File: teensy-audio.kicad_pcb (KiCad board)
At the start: 2 copper layers, 80 x 140 mm, 47 parts, among them J1 AudioJack2, J10 Conn_01x05, J11 Conn_01x02, J2 AudioJack2, J3 Barrel_Jack, J4 Conn_02x08_Odd_Even, J5 Conn_02x08_Odd_Even, J6 Conn_02x05_Odd_Even, J7 Conn_01x04, J8 Conn_01x04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

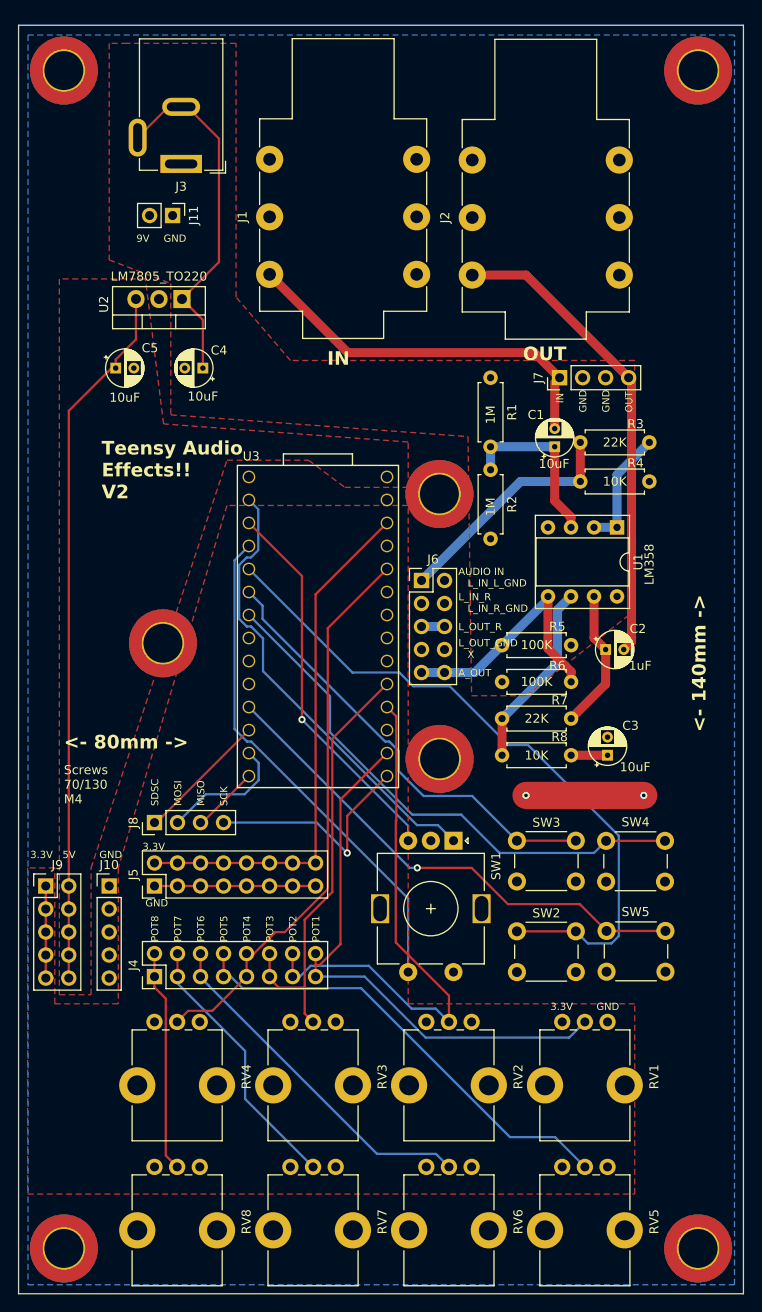
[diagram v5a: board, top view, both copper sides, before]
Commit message: added pin nubmers to silkscreen
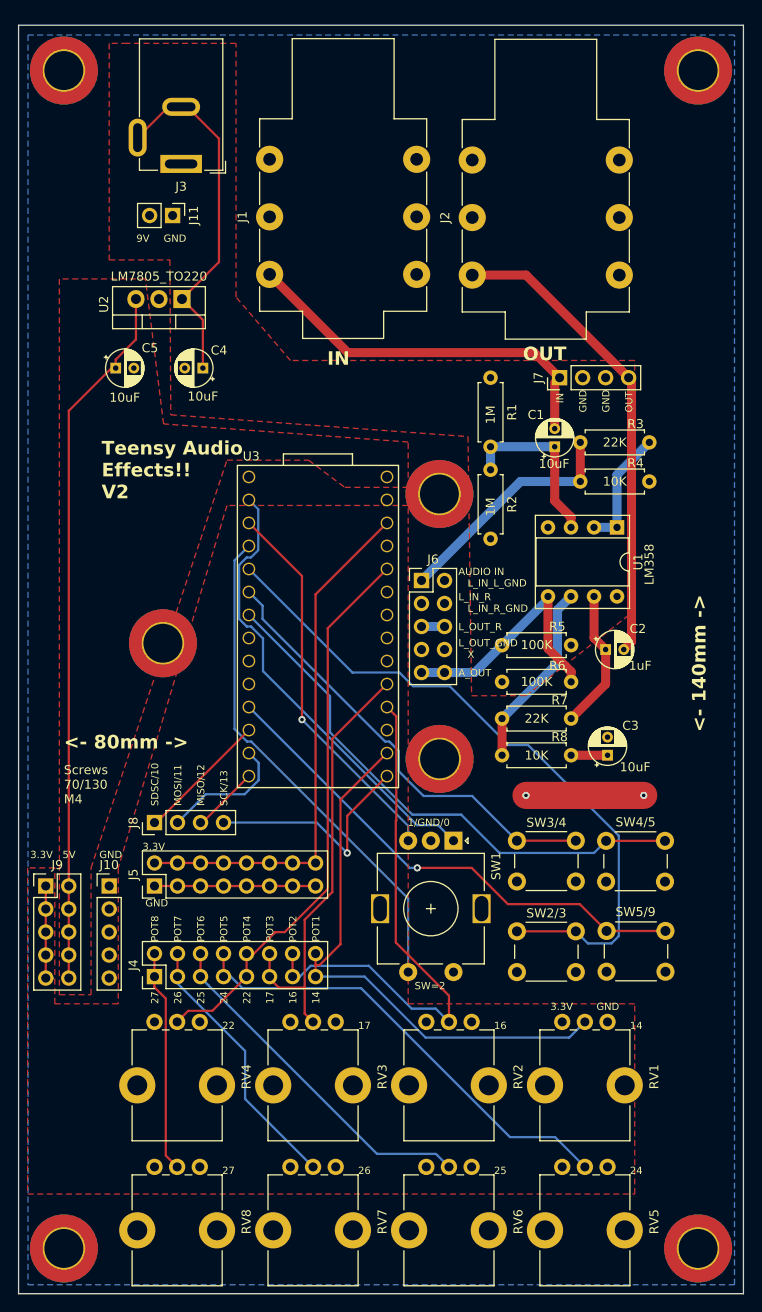
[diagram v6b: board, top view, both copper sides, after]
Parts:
- renumbered SW2 to SW2/3, SW3 to SW3/4, SW4 to SW4/5, SW5 to SW5/9
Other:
- board text added: "1/GND/0"
- board text added: "14"
- board text added: "16"
- board text added: "17"
- board text added: "22"
- board text added: "24"
- board text added: "25"
- board text added: "26"
- board text added: "27"
- board text added: "MISO/12"
- board text added: "MOSI/11"
- board text added: "SCK/13"
- board text added: "SDSC/10"
- board text added: "SW=2"
- board text removed: "MISO"
- board text removed: "MOSI"
- board text removed: "SCK"
- board text removed: "SDSC"
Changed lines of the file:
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@@
     (property "ki_keywords" "switch normally-open pushbutton push-button")
     (attr through_hole)
-    (fp_text reference "SW5" (at 3.302 6.604) (layer "F.SilkS")
+    (fp_text reference "SW5/9" (at 3.302 6.604) (layer "F.SilkS")
         (effects (font (size 1 1) (thickness 0.15)))
     )
@@
     (property "ki_keywords" "switch normally-open pushbutton push-button")
     (attr through_hole)
-    (fp_text reference "SW3" (at 3.25 -2) (layer "F.SilkS")
+    (fp_text reference "SW3/4" (at 3.25 -2) (layer "F.SilkS")
         (effects (font (size 1 1) (thickness 0.15)))
     )
@@
     (property "ki_keywords" "switch normally-open pushbutton push-button")
     (attr through_hole)
-    (fp_text reference "SW2" (at 3.25 -2) (layer "F.SilkS")
+    (fp_text reference "SW2/3" (at 3.25 -2) (layer "F.SilkS")
         (effects (font (size 1 1) (thickness 0.15)))
     )
@@
     (property "ki_keywords" "switch normally-open pushbutton push-button")
     (attr through_hole)
-    (fp_text reference "SW4" (at 3.25 6.568) (layer "F.SilkS")
+    (fp_text reference "SW4/5" (at 3.25 6.568) (layer "F.SilkS")
         (effects (font (size 1 1) (thickness 0.15)))
     )
@@
   (gr_rect (start 160 20) (end 240 160)
     (stroke (width 0.1) (type default)) (fill none) (layer "Edge.Cuts"))
-  (gr_text "SCK" (at 183.134 106.172 90) (layer "F.SilkS")
+  (gr_text "SCK/13" (at 183.134 106.172 90) (layer "F.SilkS")
+    (effects (font (size 0.8 0.8) (thickness 0.08)) (justify left bottom))
+  )
+  (gr_text "24" (at 183.134 128.016 90) (layer "F.SilkS")
     (effects (font (size 0.8 0.8) (thickness 0.08)) (justify left bottom))
   )
@@
     (effects (font (size 0.8 0.8) (thickness 0.08)) (justify left bottom))
   )
-  (gr_text "MOSI" (at 178.054 106.172 90) (layer "F.SilkS")
+  (gr_text "1/GND/0" (at 202.946 108.458) (layer "F.SilkS")
+    (effects (font (size 0.8 0.8) (thickness 0.08)) (justify left bottom))
+  )
+  (gr_text "MOSI/11" (at 178.054 106.172 90) (layer "F.SilkS")
     (effects (font (size 0.8 0.8) (thickness 0.08)) (justify left bottom))
   )
@@
     (effects (font (size 0.8 0.8) (thickness 0.08)) (justify left bottom))
   )
+  (gr_text "22" (at 185.674 128.016 90) (layer "F.SilkS")
+    (effects (font (size 0.8 0.8) (thickness 0.08)) (justify left bottom))
+  )
   (gr_text "POT8" (at 175.514 121.158 90) (layer "F.SilkS")
     (effects (font (size 0.8 0.8) (thickness 0.08)) (justify left bottom))
   )
+  (gr_text "25" (at 212.47 146.88) (layer "F.SilkS")
+    (effects (font (size 0.8 0.8) (thickness 0.08)) (justify left bottom))
+  )
   (gr_text "9V" (at 173 44) (layer "F.SilkS")
     (effects (font (size 0.8 0.8) (thickness 0.08)) (justify left bottom))
@@
     (effects (font (size 1 1) (thickness 0.15)) (justify left bottom))
   )
+  (gr_text "17" (at 188.214 128.016 90) (layer "F.SilkS")
+    (effects (font (size 0.8 0.8) (thickness 0.08)) (justify left bottom))
+  )
   (gr_text "GND" (at 168.91 112.014) (layer "F.SilkS")
     (effects (font (size 0.8 0.8) (thickness 0.08)) (justify left bottom))
@@
     (effects (font (size 0.8 0.8) (thickness 0.08)) (justify left bottom))
   )
+  (gr_text "14" (at 193.294 128.016 90) (layer "F.SilkS")
+    (effects (font (size 0.8 0.8) (thickness 0.08)) (justify left bottom))
+  )
+  (gr_text "14" (at 227.47 130.88) (layer "F.SilkS")
+    (effects (font (size 0.8 0.8) (thickness 0.08)) (justify left bottom))
+  )
   (gr_text "GND" (at 176 44) (layer "F.SilkS")
     (effects (font (size 0.8 0.8) (thickness 0.08)) (justify left bottom))
   )
+  (gr_text "25" (at 180.594 128.016 90) (layer "F.SilkS")
+    (effects (font (size 0.8 0.8) (thickness 0.08)) (justify left bottom))
+  )
   (gr_text "OUT" (at 215.646 57.15) (layer "F.SilkS")
     (effects (font (size 1.5 1.5) (thickness 0.3) bold) (justify left bottom))
   )
+  (gr_text "26" (at 197.47 146.88) (layer "F.SilkS")
+    (effects (font (size 0.8 0.8) (thickness 0.08)) (justify left bottom))
+  )
   (gr_text "GND" (at 173.99 117.348) (layer "F.SilkS")
     (effects (font (size 0.8 0.8) (thickness 0.08)) (justify left bottom))
@@
     (effects (font (size 0.8 0.8) (thickness 0.08)) (justify left bottom))
   )
-  (gr_text "SDSC" (at 175.514 106.172 90) (layer "F.SilkS")
+  (gr_text "24" (at 227.47 146.88) (layer "F.SilkS")
+    (effects (font (size 0.8 0.8) (thickness 0.08)) (justify left bottom))
+  )
+  (gr_text "SDSC/10" (at 175.514 106.172 90) (layer "F.SilkS")
+    (effects (font (size 0.8 0.8) (thickness 0.08)) (justify left bottom))
+  )
+  (gr_text "SW=2" (at 203.708 126.492) (layer "F.SilkS")
     (effects (font (size 0.8 0.8) (thickness 0.08)) (justify left bottom))
   )
@@
     (effects (font (size 0.8 0.8) (thickness 0.08)) (justify left bottom))
   )
-  (gr_text "MISO" (at 180.594 106.172 90) (layer "F.SilkS")
+  (gr_text "MISO/12" (at 180.594 106.172 90) (layer "F.SilkS")
     (effects (font (size 0.8 0.8) (thickness 0.08)) (justify left bottom))
   )
@@
     (effects (font (size 0.8 0.8) (thickness 0.08)) (justify left bottom))
   )
+  (gr_text "16" (at 190.754 128.016 90) (layer "F.SilkS")
+    (effects (font (size 0.8 0.8) (thickness 0.08)) (justify left bottom))
+  )
   (gr_text "L_IN_R" (at 208.534 83.566) (layer "F.SilkS")
     (effects (font (size 0.8 0.8) (thickness 0.08)) (justify left bottom))
@@
     (effects (font (size 0.8 0.8) (thickness 0.08)) (justify left bottom))
   )
+  (gr_text "26" (at 178.054 128.016 90) (layer "F.SilkS")
+    (effects (font (size 0.8 0.8) (thickness 0.08)) (justify left bottom))
+  )
+  (gr_text "17" (at 197.47 130.88) (layer "F.SilkS")
+    (effects (font (size 0.8 0.8) (thickness 0.08)) (justify left bottom))
+  )
   (gr_text "L_OUT_R" (at 208.534 86.868) (layer "F.SilkS")
     (effects (font (size 0.8 0.8) (thickness 0.08)) (justify left bottom))
   )
+  (gr_text "27" (at 182.47 146.88) (layer "F.SilkS")
+    (effects (font (size 0.8 0.8) (thickness 0.08)) (justify left bottom))
+  )
   (gr_text "L_IN_L_GND" (at 209.55 82.042) (layer "F.SilkS")
     (effects (font (size 0.8 0.8) (thickness 0.08)) (justify left bottom))
   )
+  (gr_text "27" (at 175.514 128.016 90) (layer "F.SilkS")
+    (effects (font (size 0.8 0.8) (thickness 0.08)) (justify left bottom))
+  )
+  (gr_text "16" (at 212.47 130.88) (layer "F.SilkS")
+    (effects (font (size 0.8 0.8) (thickness 0.08)) (justify left bottom))
+  )
   (gr_text "<- 80mm ->" (at 165 100) (layer "F.SilkS")
     (effects (font (size 1.5 1.5) (thickness 0.25) bold) (justify left bottom))
   )
+  (gr_text "22" (at 182.47 130.88) (layer "F.SilkS")
+    (effects (font (size 0.8 0.8) (thickness 0.08)) (justify left bottom))
+  )
   (gr_text "AUDIO IN" (at 208.534 80.772) (layer "F.SilkS")
     (effects (font (size 0.8 0.8) (thickness 0.08)) (justify left bottom))
@@
         (xy 170 22)
         (xy 170 45.9)
-        (xy 176.8 48.5)
+        (xy 176.7 45.9)
         (xy 176.8 63)
         (xy 209.6 65.4)

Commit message: removed bridged ground plane
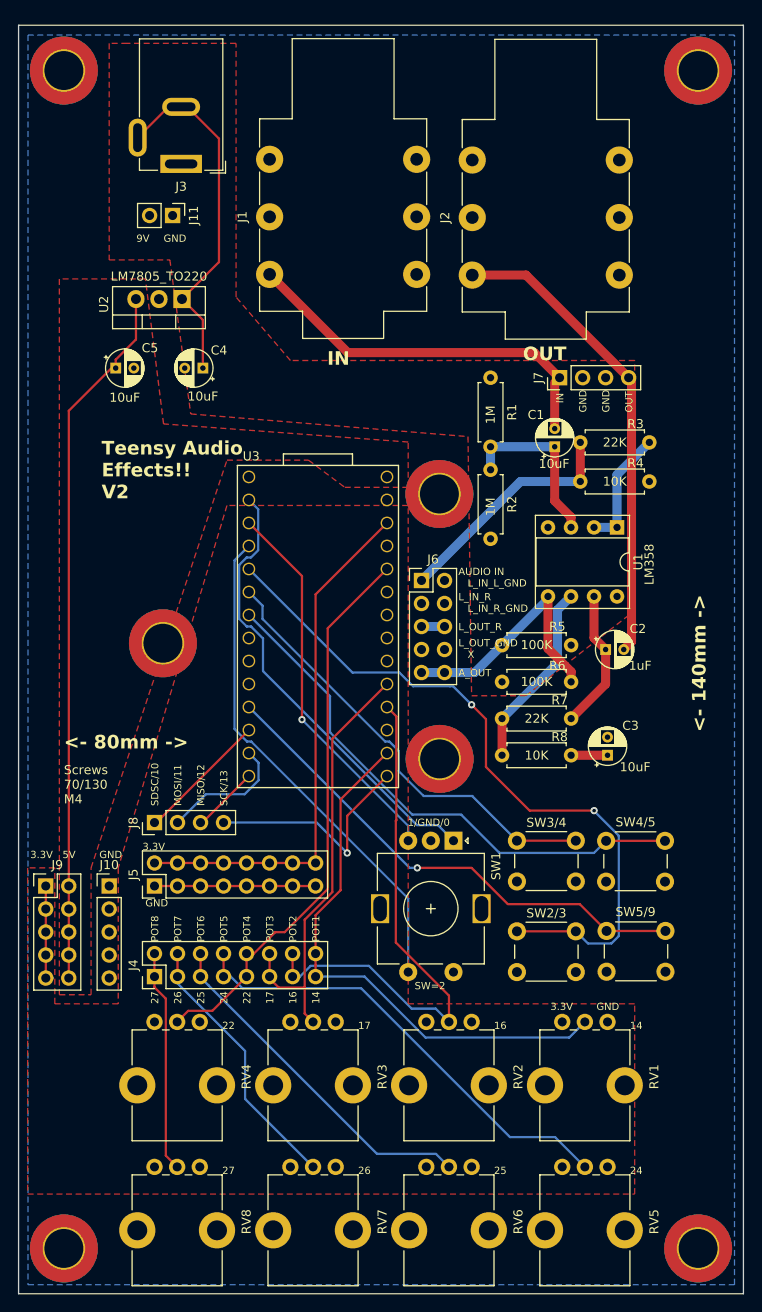
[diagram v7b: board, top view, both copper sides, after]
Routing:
- net GND: track 30.8 -> 17.8 mm, vias 2 -> 0
- net SW2: track 76.2 -> 79.3 mm, vias 0 -> 2
- net POT1: track 62.7 -> 61.2 mm
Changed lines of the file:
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@@
   (segment (start 219.48 90.4) (end 219.48 84.53) (width 1) (layer "B.Cu") (net 9))
   (segment (start 192.78 123.73) (end 192.78 125) (width 0.25) (layer "F.Cu") (net 10))
-  (segment (start 193.221 123.73) (end 195.53 121.42) (width 0.25) (layer "F.Cu") (net 10))
-  (segment (start 195.53 105.46) (end 200.66 100.33) (width 0.25) (layer "F.Cu") (net 10))
-  (segment (start 195.53 121.42) (end 195.53 105.46) (width 0.25) (layer "F.Cu") (net 10))
+  (segment (start 192.78 122.46) (end 192.78 118.22) (width 0.25) (layer "F.Cu") (net 10))
+  (segment (start 192.78 118.22) (end 195.5434 115.4566) (width 0.25) (layer "F.Cu") (net 10))
+  (segment (start 195.5434 115.4566) (end 195.5434 105.4466) (width 0.25) (layer "F.Cu") (net 10))
   (segment (start 192.78 122.46) (end 192.78 123.73) (width 0.25) (layer "F.Cu") (net 10))
-  (segment (start 192.78 123.73) (end 193.221 123.73) (width 0.25) (layer "F.Cu") (net 10))
+  (segment (start 195.5434 105.4466) (end 200.66 100.33) (width 0.25) (layer "F.Cu") (net 10))
   (segment (start 222.5 130) (end 220.77 131.73) (width 0.25) (layer "B.Cu") (net 10))
   (segment (start 220.77 131.73) (end 204.918 131.73) (width 0.25) (layer "B.Cu") (net 10))
@@
   (segment (start 183.84 97.6831) (end 185.217 99.06) (width 0.25) (layer "B.Cu") (net 33))
   (segment (start 183.84 79.0496) (end 183.84 97.6831) (width 0.25) (layer "B.Cu") (net 33))
+  (segment (start 211.582 101.854) (end 216.408 106.68) (width 0.25) (layer "F.Cu") (net 34))
+  (segment (start 216.408 106.68) (end 223.52 106.68) (width 0.25) (layer "F.Cu") (net 34))
+  (segment (start 210 95) (end 211.582 96.582) (width 0.25) (layer "F.Cu") (net 34))
   (segment (start 215 120) (end 221.5 120) (width 0.25) (layer "F.Cu") (net 34))
-  (segment (start 226.243 109.449) (end 216.238 99.4446) (width 0.25) (layer "B.Cu") (net 34))
+  (segment (start 211.582 96.582) (end 211.582 101.854) (width 0.25) (layer "F.Cu") (net 34))
+  (via (at 210 95) (size 0.8) (drill 0.4) (layers "F.Cu" "B.Cu") (net 34))
+  (via (at 223.52 106.68) (size 0.8) (drill 0.4) (layers "F.Cu" "B.Cu") (net 34))
+  (segment (start 207.9548 92.9548) (end 210 95) (width 0.25) (layer "B.Cu") (net 34))
   (segment (start 196.85 91.44) (end 185.42 80.01) (width 0.25) (layer "B.Cu") (net 34))
   (segment (start 203.538 92.9548) (end 202.023 91.44) (width 0.25) (layer "B.Cu") (net 34))
-  (segment (start 214.09 99.4446) (end 207.6 92.9548) (width 0.25) (layer "B.Cu") (net 34))
   (segment (start 226.243 120.521) (end 226.243 109.449) (width 0.25) (layer "B.Cu") (net 34))
+  (segment (start 223.52 106.68) (end 223.52 106.726) (width 0.25) (layer "B.Cu") (net 34))
   (segment (start 207.6 92.9548) (end 203.538 92.9548) (width 0.25) (layer "B.Cu") (net 34))
+  (segment (start 207.6 92.9548) (end 207.9548 92.9548) (width 0.25) (layer "B.Cu") (net 34))
+  (segment (start 223.52 106.726) (end 226.243 109.449) (width 0.25) (layer "B.Cu") (net 34))
   (segment (start 221.5 120) (end 222.835 121.335) (width 0.25) (layer "B.Cu") (net 34))
   (segment (start 225.429 121.335) (end 226.243 120.521) (width 0.25) (layer "B.Cu") (net 34))
-  (segment (start 216.238 99.4446) (end 214.09 99.4446) (width 0.25) (layer "B.Cu") (net 34))
   (segment (start 202.023 91.44) (end 196.85 91.44) (width 0.25) (layer "B.Cu") (net 34))
   (segment (start 222.835 121.335) (end 225.429 121.335) (width 0.25) (layer "B.Cu") (net 34))
@@
   (segment (start 182.62 115) (end 180.08 115) (width 0.25) (layer "F.Cu") (net 46))
   (segment (start 177.54 115) (end 175 115) (width 0.25) (layer "F.Cu") (net 46))
-  (segment (start 216 105) (end 229 105) (width 3) (layer "F.Cu") (net 46))
   (segment (start 192.78 115) (end 190.24 115) (width 0.25) (layer "F.Cu") (net 46))
   (segment (start 185.16 115) (end 182.62 115) (width 0.25) (layer "F.Cu") (net 46))
   (segment (start 187.7 115) (end 185.16 115) (width 0.25) (layer "F.Cu") (net 46))
-  (via (at 229 105) (size 0.8) (drill 0.4) (layers "F.Cu" "B.Cu") (free) (net 46))
-  (via (at 216 105) (size 0.8) (drill 0.4) (layers "F.Cu" "B.Cu") (free) (net 46))
   (segment (start 220.478 145.522) (end 220 146) (width 0.25) (layer "F.Cu") (net 47))
   (segment (start 175 112.46) (end 175 112.805) (width 0.25) (layer "F.Cu") (net 47))
@@
         (xy 170 45.9)
         (xy 176.7 45.9)
-        (xy 176.8 63)
+        (xy 179 62.9)
         (xy 209.6 65.4)
         (xy 210 94)

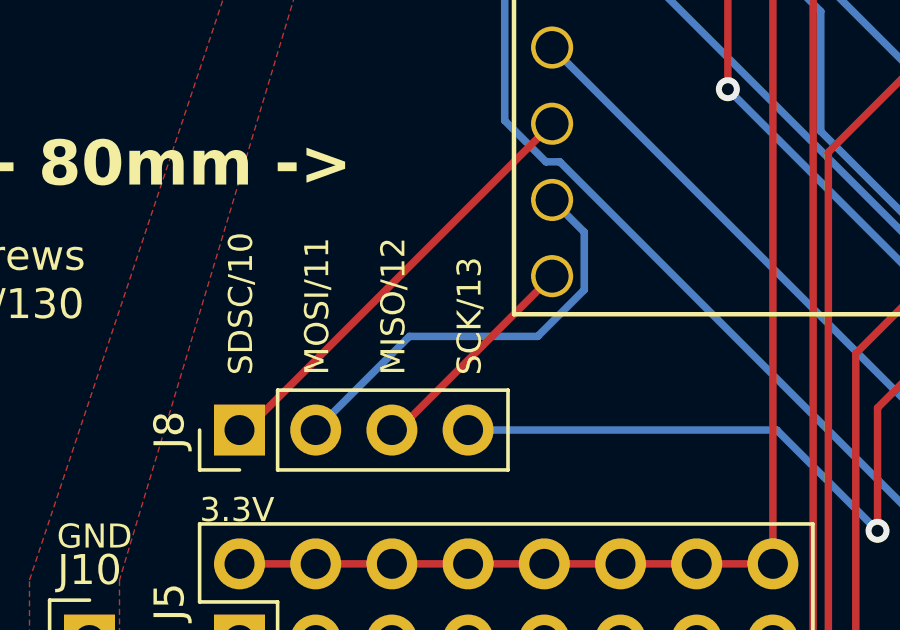
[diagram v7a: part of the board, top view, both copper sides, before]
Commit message: minor routing simplification
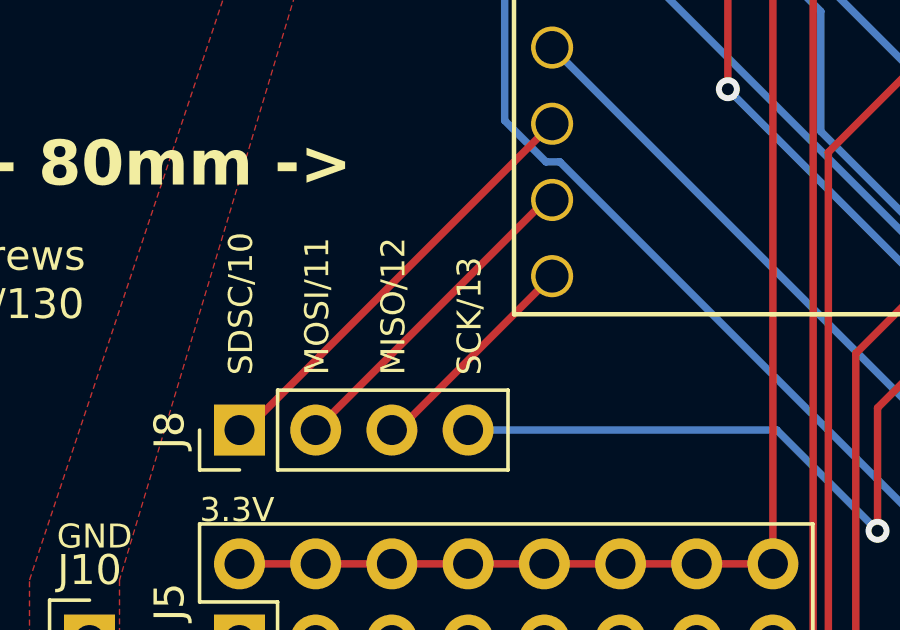
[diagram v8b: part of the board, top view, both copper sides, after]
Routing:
- net MOSI: track 14.3 -> 11.1 mm
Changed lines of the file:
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@@
   (segment (start 192.9099 108) (end 182.62 108) (width 0.25) (layer "B.Cu") (net 23))
   (segment (start 196.2684 111.3585) (end 192.9099 108) (width 0.25) (layer "B.Cu") (net 23))
-  (segment (start 180.6624 104.8776) (end 184.9423 104.8776) (width 0.25) (layer "B.Cu") (net 30))
-  (segment (start 186.4934 101.4034) (end 186.4934 103.3265) (width 0.25) (layer "B.Cu") (net 30))
-  (segment (start 177.54 108) (end 180.6624 104.8776) (width 0.25) (layer "B.Cu") (net 30))
-  (segment (start 186.4934 103.3265) (end 184.9423 104.8776) (width 0.25) (layer "B.Cu") (net 30))
-  (segment (start 185.42 100.33) (end 186.4934 101.4034) (width 0.25) (layer "B.Cu") (net 30))
+  (segment (start 185.21 100.33) (end 185.42 100.33) (width 0.25) (layer "F.Cu") (net 30))
+  (segment (start 177.54 108) (end 185.21 100.33) (width 0.25) (layer "F.Cu") (net 30))
   (segment (start 186.981 91.2891) (end 186.981 87.6731) (width 0.25) (layer "B.Cu") (net 31))
   (segment (start 186.981 87.6731) (end 185.668 86.36) (width 0.25) (layer "B.Cu") (net 31))
